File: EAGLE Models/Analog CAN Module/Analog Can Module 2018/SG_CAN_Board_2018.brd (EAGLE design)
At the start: 160 x 100 mm, 110 parts, among them IC1 AT90CAN128, IC2 MCP2551SO8, IC3 NUP2105L, IC5 FT232RL, Q1 56P2859, U1 LTC2053, U11 LTC2053, U12 LTC2053, U2 LTC2053, U3 LTC2053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

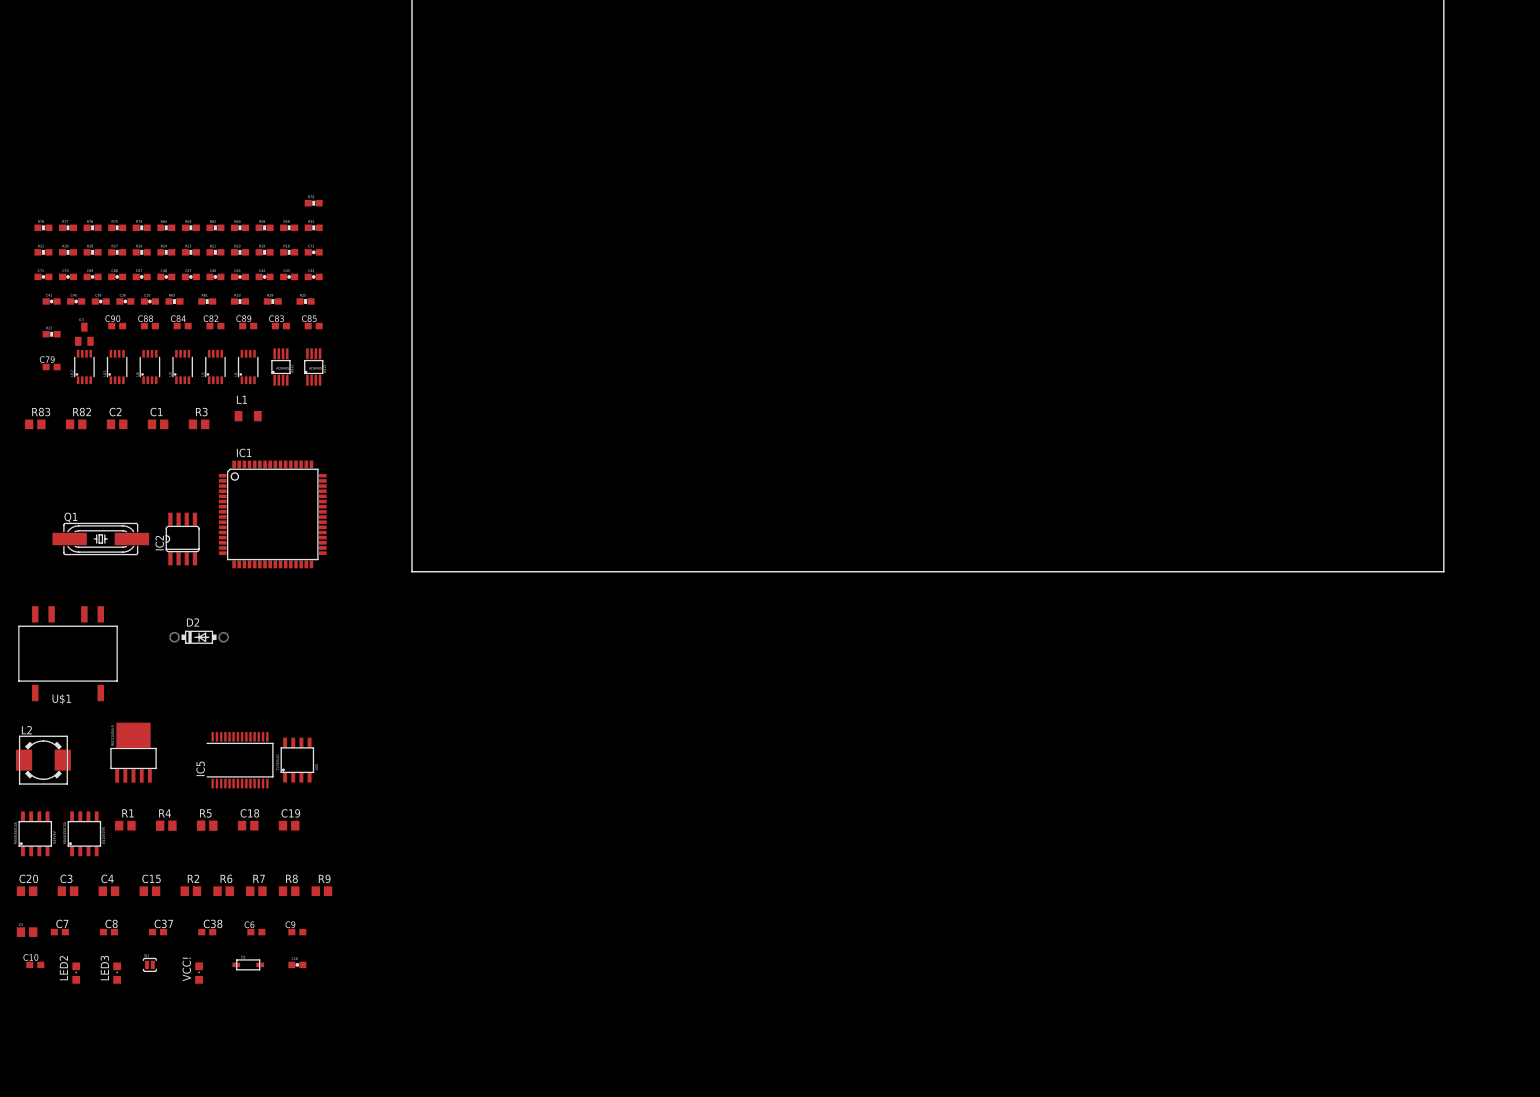
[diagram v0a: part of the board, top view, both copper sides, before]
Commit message: Updated SG CAN schematic and started analog CAN schematic
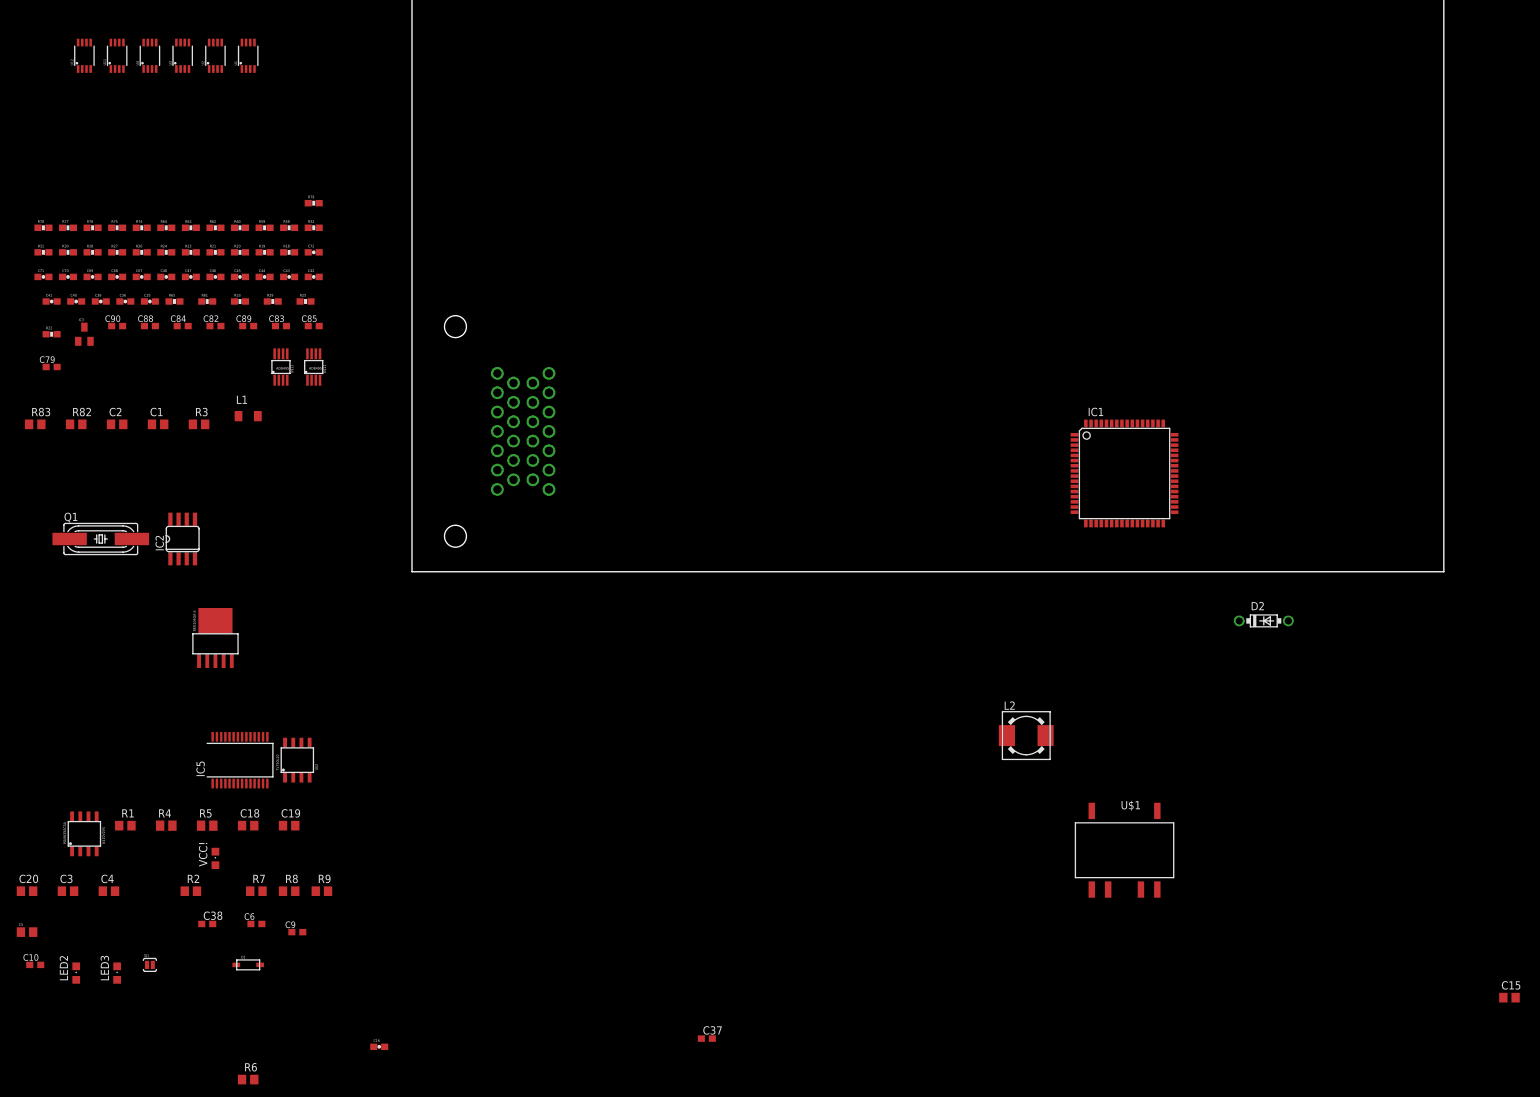
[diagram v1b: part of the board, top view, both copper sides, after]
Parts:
- removed C7, C8: 2.2uF, rcl:C0603@1
- removed U$4V5V: MAX6350CSA, DashAndCAN library:8-SOIC
- added U$3: SUPERSEAL1.0_26POS, TE:SUPERSEAL1.0_26POS
- moved C15 211.5 mm to (170.2, -66.0)
- moved U$1 166.6 mm to (110.5, -43.2), turned to 180 degrees
- moved D2 165.1 mm to (132.1, -7.62)
- moved L2 152.4 mm to (95.2, -25.4)
- moved IC1 132.2 mm to (110.5, 15.2)
- moved C37 86.7 mm to (45.7, -72.4)
- moved U1 48.3 mm to (-25.4, 80.0)
- moved U11 48.3 mm to (-45.7, 80.0)
- moved U12 48.3 mm to (-50.8, 80.0)
- moved U2 48.3 mm to (-30.5, 80.0)
- moved U3 48.3 mm to (-35.6, 80.0)
- moved U4 48.3 mm to (-40.6, 80.0)
- moved R6 29.5 mm to (-25.4, -78.7)
- moved U$5 21.8 mm to (-30.5, -7.62)
- moved C16 18.0 mm to (-5.08, -73.7)
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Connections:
- removed net 5VREF: C8.1, U$4V5V.P6
- removed net PF0: IC1.61
- removed net PF1: IC1.60
- removed net PF2: IC1.59
- removed net PF3: IC1.58
- removed net SGO11: C67.1, C69.2, R61.2, U11.7
- removed net SGO12: C70.1, C72.2, R65.2, U12.7
- removed net SG_11: U11.2
- removed net SG_12: U12.2
- removed net TCK: IC1.57
- removed net TDI: IC1.54
- removed net TDO: IC1.55
- removed net TMS: IC1.56
- new net N$18: U$3.B18
- new net N$19: U$3.B19
- new net N$46: U$3.B7
- new net N$47: U$3.B6
- new net SGO5: C67.1, C69.2, IC1.57, R61.2, U11.7
- new net SGO6: C70.1, C72.2, IC1.56, R65.2, U12.7
- new net SG_5: U$3.B12, U11.2
- new net SG_6: U$3.B13, U12.2
- net 10V: now also U$3.B4, U$3.B5
- net 12V: now also U$3.B1; no longer C7.1, U$4V5V.P2
- net CAN_H: now also U$3.B20
- net CAN_L: now also U$3.B21
- net GND: now also U$3.B22, U$3.B23, U$3.B24, U$3.B25, U$3.B26; no longer C7.2, C8.2, U$4V5V.P4
- net SGO1: now also IC1.61
- net SGO2: now also IC1.60
- net SGO3: now also IC1.59
- net SGO4: now also IC1.58
- net SG_1: now also U$3.B8
- net SG_2: now also U$3.B9
- net SG_3: now also U$3.B10
- net SG_4: now also U$3.B11
- net TCI1+: now also U$3.B14
- net TCI1-: now also U$3.B15
- net TCI2+: now also U$3.B16
- net TCI2-: now also U$3.B17
- net TCO1: now also IC1.55
- net TCO2: now also IC1.54
- net VCC: now also U$3.B2, U$3.B3

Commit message: SG and Analog CAN Schematics
updated schematics with usb mini connector, first draft almost complete
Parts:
- removed R82, R83: 4.7k, rcl:R0805
- added U$4: 1734753-1, con-tyco:1734753-1
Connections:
- new net N$3: U$4.P$4
- net D+: now also U$4.P$3
- net D-: now also U$4.P$2
- net GND: now also U$4.P$5
- net SCL: no longer R83.1
- net SDA: no longer R82.1
- net VCC: now also U$4.P$1; no longer R82.2, R83.2

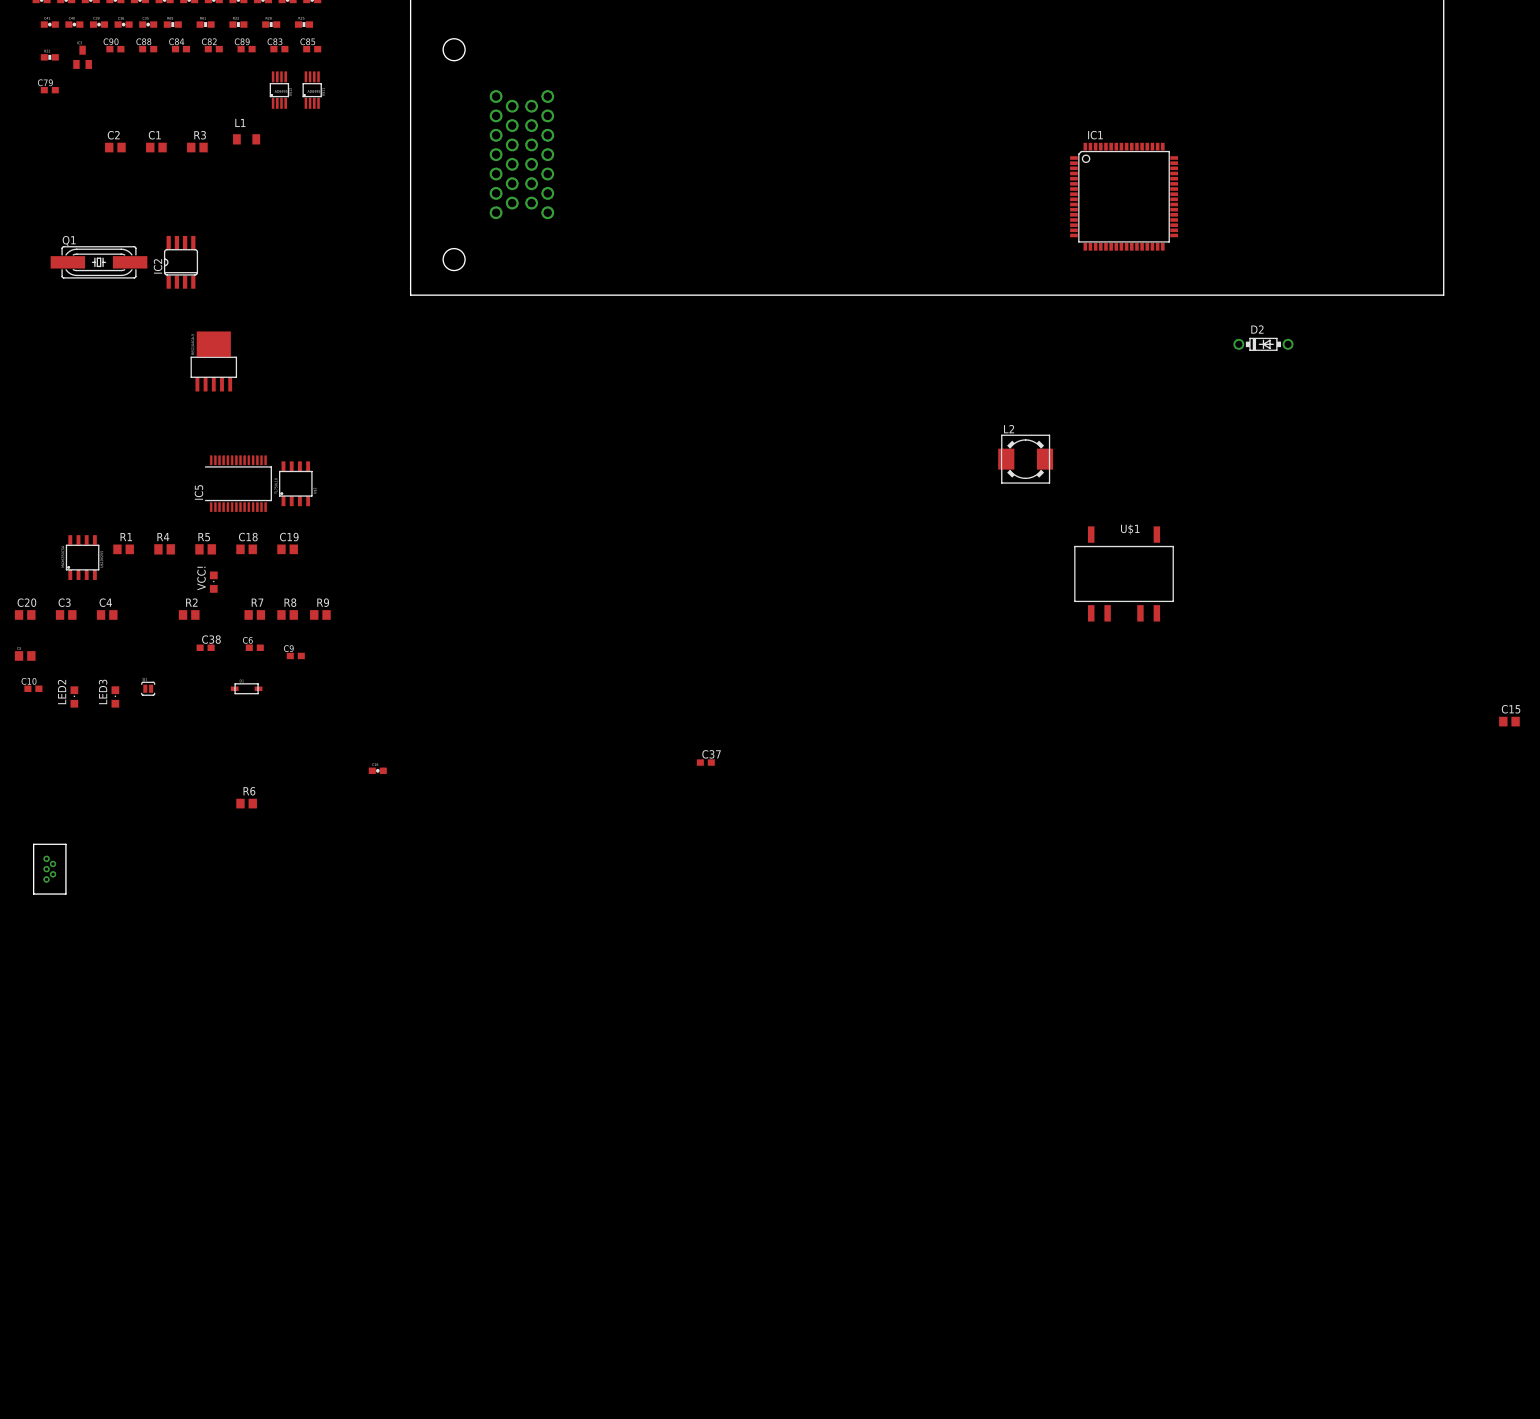
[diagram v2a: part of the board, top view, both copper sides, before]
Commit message: Updated CAN Boards
changed vcc voltage regulator
deleted 10V supply
added solder jumper
added reverse voltage protection circuit
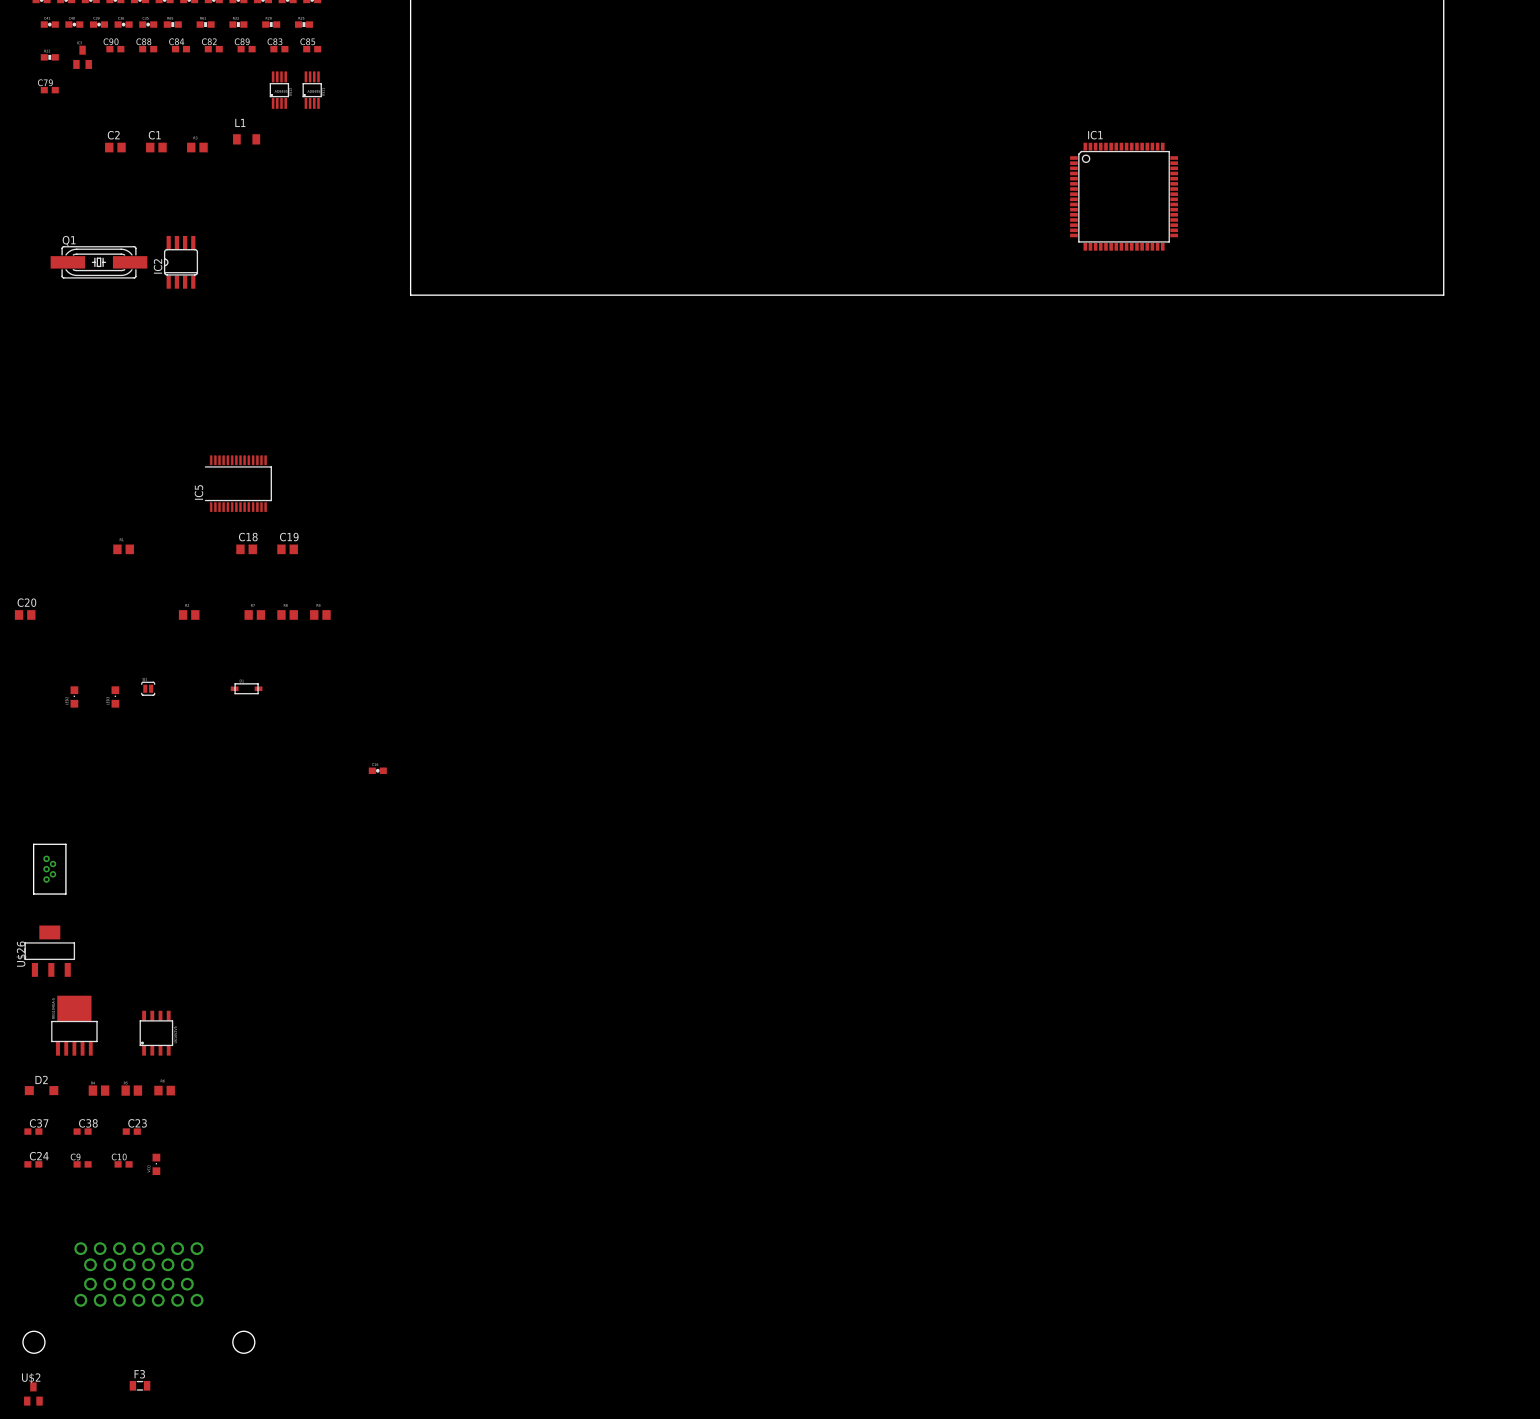
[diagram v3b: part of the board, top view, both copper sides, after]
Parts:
- removed C15: 10uF, resistor:C0805
- removed C3, C4: 22uF, resistor:C0805
- removed C5: 10uF, rcl:C0805
- removed C6: 0.1uF, rcl:C0603
- removed L2: 22uH, inductors:DR73
- removed U$1: V7805-1000, formula electric:V78XX-1000
- added C23, C24: 10uF, rcl:C0603
- added F3: 0805L050, LittleFuse:0805L
- added U$26: NCP1117, on-semiconductor:SOT-223-4
- C1, C18, C19, C2, C20: device rcl:C0805@1 -> rcl:C0805
- C10, C79, C82, C83, C84, C85, C88, C89, C9, C90: device rcl:C0603 -> rcl:C0603@1
- C37, C38: device rcl:C0603@1 -> rcl:C0603
- D2: device diode:DO41-7.6 -> diode:SOD123
- U$2: value TL750L10 -> MMBD4448H-7-F; device DashAndCAN library:8-SOIC -> diodes-inc:SOT23-3
- moved D2 221.7 mm to (-57.1, -123.2)
- moved U$3 183.5 mm to (-41.9, -152.4), turned to 0 degrees
- moved U$2 146.7 mm to (-58.4, -170.2)
- moved C37 118.8 mm to (-58.4, -129.5)
- moved U$5 105.1 mm to (-52.1, -110.5)
- moved VCC! 90.6 mm to (-39.4, -134.6)
- moved C9 85.4 mm to (-50.8, -134.6)
- moved R5 84.6 mm to (-43.2, -123.2)
- moved R4 84.4 mm to (-48.3, -123.2)
- moved C38 77.3 mm to (-50.8, -129.5)
- moved C10 75.0 mm to (-44.5, -134.6)
- moved U$10V2V5 74.5 mm to (-39.4, -114.3)
- moved R6 46.2 mm to (-38.1, -123.2)
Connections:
- removed net 12V_PROTECTED: C15.1, D2.C, U$1.1
- removed net N$13: C3.1, L2.1, U$1.5
- removed net N$18: U$3.B18
- removed net N$19: U$3.B19
- removed net N$46: U$3.B7
- removed net N$47: U$3.B6
- new net 12V_PREPTC: F3.2, U$2.3
- new net 5V_REG_IN: C23.1, D2.C, U$26.3
- net 10V: no longer C5.1, U$2.P1, U$3.B4, U$3.B5
- net 12V: now also F3.1; no longer C6.1, U$2.P8, U$3.B1
- net GND: now also C23.2, C24.2, U$2.1, U$26.1; no longer C15.2, C3.2, C4.2, C5.2, C6.2, U$1.7, U$1.9, U$2.P2, U$2.P3, U$2.P6, U$2.P7
- net PA0: now also U$3.B18
- net PA1: now also U$3.B19
- net SG_1: no longer U$3.B8
- net SG_2: no longer U$3.B9
- net SG_3: no longer U$3.B10
- net SG_4: no longer U$3.B11
- net SG_5: no longer U$3.B12
- net SG_6: no longer U$3.B13
- net VCC: now also C24.1, U$26.2, U$26.4; no longer C4.1, L2.2, U$3.B2, U$3.B3

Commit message: SG CAN Board Layout
grouped components together
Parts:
- moved C37 253.3 mm to (69.8, 88.9)
- moved C38 252.7 mm to (76.2, 88.9)
- moved C9 252.3 mm to (55.9, 94.0)
- moved C24 247.6 mm to (30.5, 96.5)
- moved R4 244.3 mm to (55.9, 97.8)
- moved C10 243.8 mm to (55.9, 87.6)
- moved U$10V2V5 237.5 mm to (72.4, 95.2), turned to 90 degrees
- moved R5 235.7 mm to (59.7, 88.9)
- moved C23 232.5 mm to (29.2, 91.4)
- moved VCC! 231.0 mm to (14.0, 90.2)
- moved D2 227.1 mm to (30.5, 86.4)
- moved U$5 225.0 mm to (44.5, 92.7), turned to 90 degrees
- moved R6 224.9 mm to (15.2, 95.2)
- moved U$3 212.3 mm to (15.2, 52.1), turned to 270 degrees
- moved U$26 209.7 mm to (22.9, 92.7), turned to 90 degrees
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
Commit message: Board Layout Edits SG CAN board
placed components on board
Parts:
- moved C71 213.4 mm to (153.7, 78.7)
- moved C70 209.5 mm to (154.9, 68.6)
- moved R78 208.7 mm to (147.3, 95.2)
- moved F3 202.5 mm to (6.35, 82.5)
- moved U12 200.8 mm to (149.9, 73.7), turned to 90 degrees
- moved C90 200.3 mm to (147.3, 91.4)
- moved U$2 199.6 mm to (6.35, 76.2)
- moved R65 194.2 mm to (154.9, 72.4), turned to 180 degrees
- moved R64 188.7 mm to (149.9, 69.8), turned to 90 degrees
- moved R77 188.6 mm to (130.8, 94.0)
- moved C69 185.2 mm to (133.3, 74.9)
- moved R63 180.0 mm to (144.8, 71.1), turned to 90 degrees
- moved C68 179.6 mm to (130.8, 78.7), turned to 180 degrees
- moved C88 179.2 mm to (130.8, 90.2)
- moved C79 178.7 mm to (114.3, 86.4)
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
